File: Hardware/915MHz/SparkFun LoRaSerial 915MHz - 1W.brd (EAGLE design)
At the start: 50.8 x 27.9 mm, 75 parts, among them J1 QWIIC_RIGHT_ANGLE, J3 USB C, J4 JTAG, U2 ATSAMD21G-A, U3 AP2112K-3.3, U4 E19-915M30S, Y1 32.768kHz

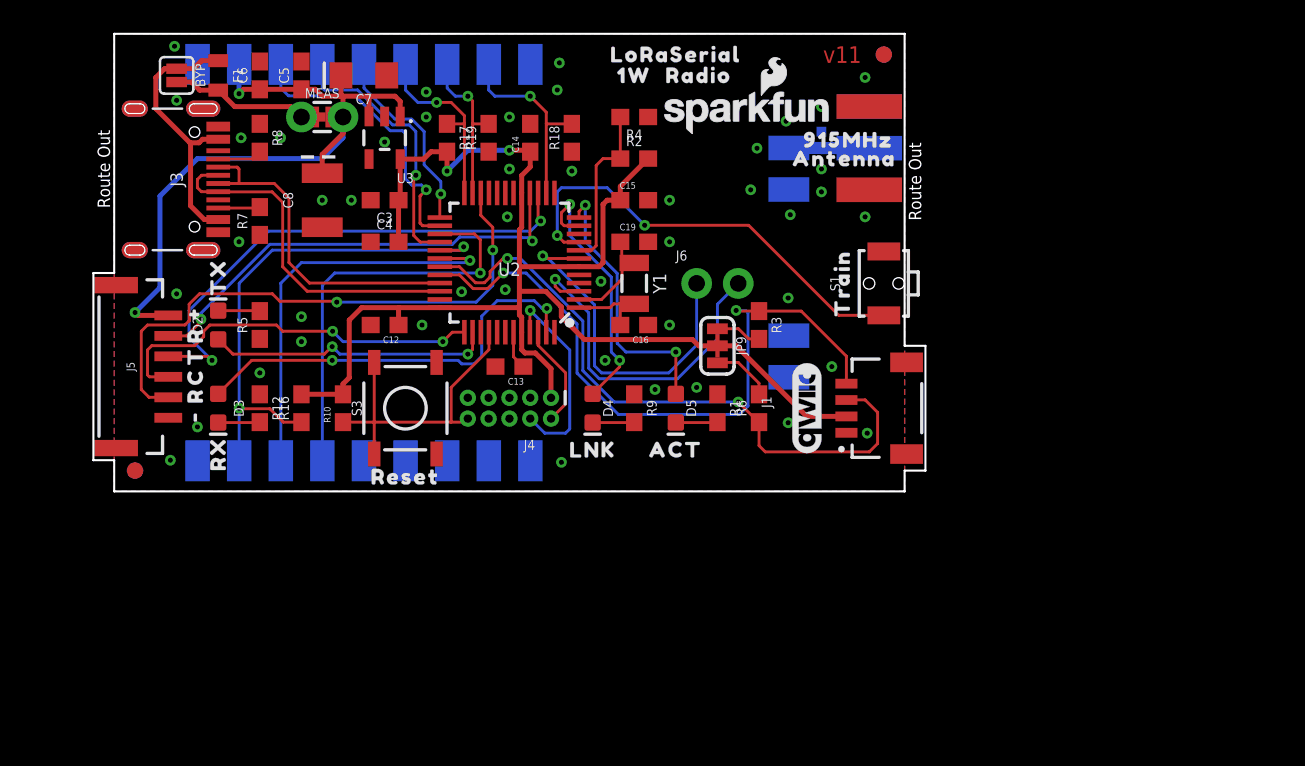
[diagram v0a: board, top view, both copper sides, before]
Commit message: Add sub folders for other frequencies
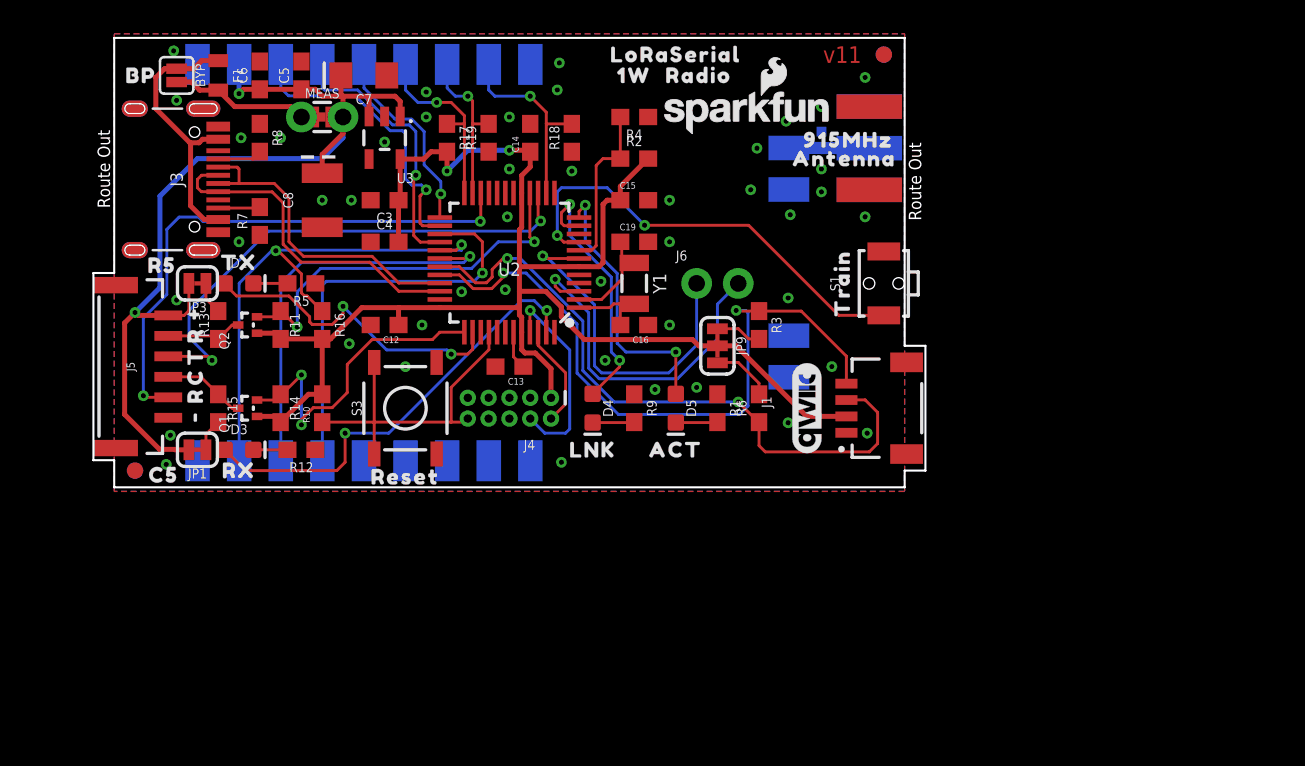
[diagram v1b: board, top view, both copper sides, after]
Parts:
- added JP1, JP3: JUMPER-SMT_2_NC_TRACE_SILK, SparkFun-Jumpers:SMT-JUMPER_2_NC_TRACE_SILK
- added Q1, Q2: 20V/0.2A/8MHz/1.2Ω/1Vth, SparkFun-DiscreteSemi:SOT-416FL
- added R11, R13, R14, R15: 2.2k, SparkFun-Resistors:0603
- added U$19: (no value), output:C50
- added U$20: (no value), output:R50
- added U$8: (no value), output:BP0
- moved R16 5.24 mm to (14.0, 10.2), turned to 270 degrees
- moved R12 3.59 mm to (12.7, 2.54), turned to 180 degrees
- moved R5 3.59 mm to (12.7, 12.7), turned to 180 degrees
- moved D3 2.84 mm to (8.89, 2.54), turned to 0 degrees
- moved D2 2.84 mm to (8.89, 12.7), turned to 0 degrees
- moved U$10 1.63 mm to (8.89, 1.27), turned to 0 degrees
- moved U$11 1.55 mm to (8.89, 14.0), turned to 0 degrees
- moved R10 1.27 mm to (14.0, 5.08)
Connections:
- removed net D30/CTS-I: J5.4, U2.37
- removed net RX-I: J5.2, U2.16
- new net CTS-I_HV: J5.4, Q1.3, R15.1
- new net D30/CTS-I_LV: Q1.2, R14.1, U2.37
- new net N$5: JP3.1, R13.2
- new net N$6: JP1.1, R15.2
- new net RX-I_HV: J5.2, Q2.3, R13.1
- new net RX-I_LV: Q2.2, R11.1, U2.16
- net 3.3V: now also Q1.1, Q2.1, R11.2, R14.2
- net 5V: now also JP1.2, JP3.2
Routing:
- net RX-I: track 28.1 -> 0.00 mm, vias 2 -> 0
- net RX-I_LV: track 0.00 -> 24.0 mm, vias 0 -> 2
- net D30/CTS-I: track 23.7 -> 0.00 mm, vias 2 -> 0
- net D30/CTS-I_LV: track 0.00 -> 19.9 mm, vias 0 -> 2
- net 5V: track 45.3 -> 59.6 mm
- net 3.3V: track 87.1 -> 94.4 mm
- net CTS-I_HV: track 0.00 -> 5.06 mm
- net RX-I_HV: track 0.00 -> 4.70 mm
- net D31/TX_LED: track 17.5 -> 19.5 mm
- net N$6: track 0.00 -> 2.00 mm
- net N$5: track 0.00 -> 2.00 mm
- net A5/RX_LED: track 25.7 -> 27.1 mm
- net D38/RTS-O: track 35.0 -> 33.6 mm
- net SAMD_!RESET!: track 19.8 -> 21.1 mm
- net D6/LORA_!RST!: track 31.3 -> 32.1 mm
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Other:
- board size 50.8 x 27.9 mm -> 50.8 x 27.4 mm

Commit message: Add RSSI LEDs
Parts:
- added D1, D7, D8: GREEN, SparkFun-LED:LED-0603
- added R20, R21, R22: 4.7k, SparkFun-Resistors:0603
- added U$21: (no value), output:RSSI0
- added U$22: (no value), output:10
- added U1: ESP32, SparkFun-RF:QFN48-0.4MM
- added U5: ESP-WROOM-3232D, SparkFun-RF:ESP-WROOM-32D
- D2: value GREEN -> BLUE
- D4: value BLUE -> GREEN
- R5: value 4.7k -> 1k
- R9: value 1k -> 4.7k
- U$6: device output:ACT3 -> output:01
- U$7: device output:LNK2 -> output:PWR0
- moved R1 21.9 mm to (17.8, 13.3), turned to 180 degrees
- moved D5 20.4 mm to (17.8, 15.0), turned to 180 degrees
- moved U$7 20.2 mm to (14.2, 14.5)
- moved U$6 12.5 mm to (39.4, 14.5)
- moved R9 3.81 mm to (33.0, 1.27), turned to 0 degrees
- moved D4 3.81 mm to (34.3, 5.08)
- moved R6 2.84 mm to (41.9, 7.62), turned to 180 degrees
- moved C4 1.40 mm to (17.8, 16.6)
- moved R3 1.27 mm to (41.9, 10.2), turned to 180 degrees
- moved LOGO3 0.76 mm to (44.3, 5.08)
- moved C3 0.63 mm to (17.8, 18.4)
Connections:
- removed net A3/TRAIN: S1.1, U2.9
- removed net A4: U2.10
- removed net D4: U2.13
- removed net D8/LINK: D4.A, U2.11
- removed net D9/ACT: D5.A, U2.12
- new net A3/RSSI1: D1.A, U2.9
- new net A4/RSSI2: D4.A, U2.10
- new net D4/TRAIN: S1.1, U2.13
- new net D8/RSSI3: D7.A, U2.11
- new net D9/RSSI4: D8.A, U2.12
- new net N$10: D7.C, R21.2
- new net N$11: D8.C, R22.2
- new net N$9: D1.C, R20.2
- net 3.3V: now also D5.A
- net GND: now also R20.1, R21.1, R22.1
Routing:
- net D4/TRAIN: track 0.00 -> 33.1 mm
- net A3/TRAIN: track 27.4 -> 0.00 mm, vias 2 -> 0
- net D8/RSSI3: track 0.00 -> 20.9 mm, vias 0 -> 2
- net D9/RSSI4: track 0.00 -> 20.8 mm, vias 0 -> 2
- net D9/ACT: track 16.5 -> 0.00 mm, vias 2 -> 0
- net D8/LINK: track 16.0 -> 0.00 mm, vias 2 -> 0
- net A4/RSSI2: track 0.00 -> 14.4 mm, vias 0 -> 2
- net A3/RSSI1: track 0.00 -> 13.3 mm, vias 0 -> 2
- net D21/SCL: track 41.3 -> 37.6 mm
- net N$9: track 0.00 -> 3.11 mm
- net N$10: track 0.00 -> 3.11 mm
- net N$11: track 0.00 -> 3.11 mm
- net D20/SDA: track 39.9 -> 37.7 mm, vias 2 -> 3
- net 3.3V: track 94.4 -> 95.9 mm
- net N$7: track 2.55 -> 1.66 mm
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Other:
- board text added: "v12"
- board text removed: "v11"

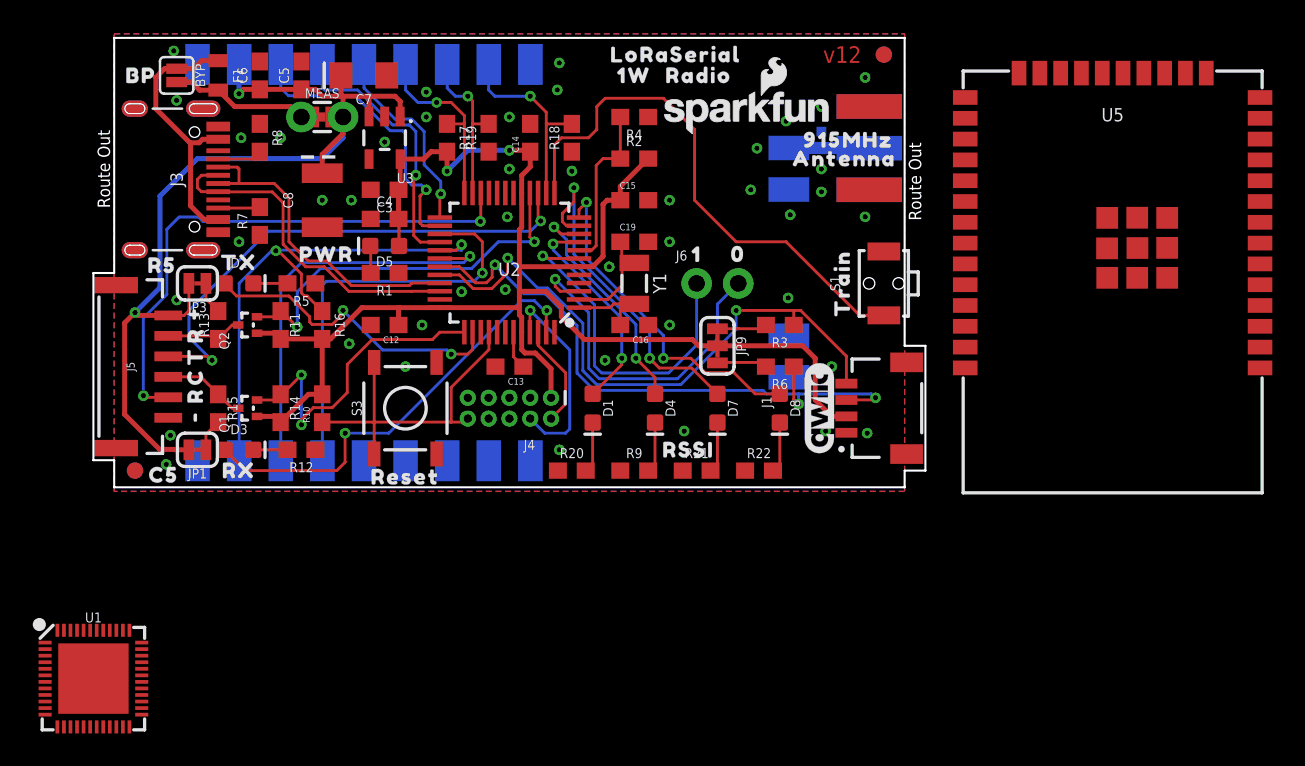
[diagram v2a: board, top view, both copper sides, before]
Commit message: Add RSSI LEDs
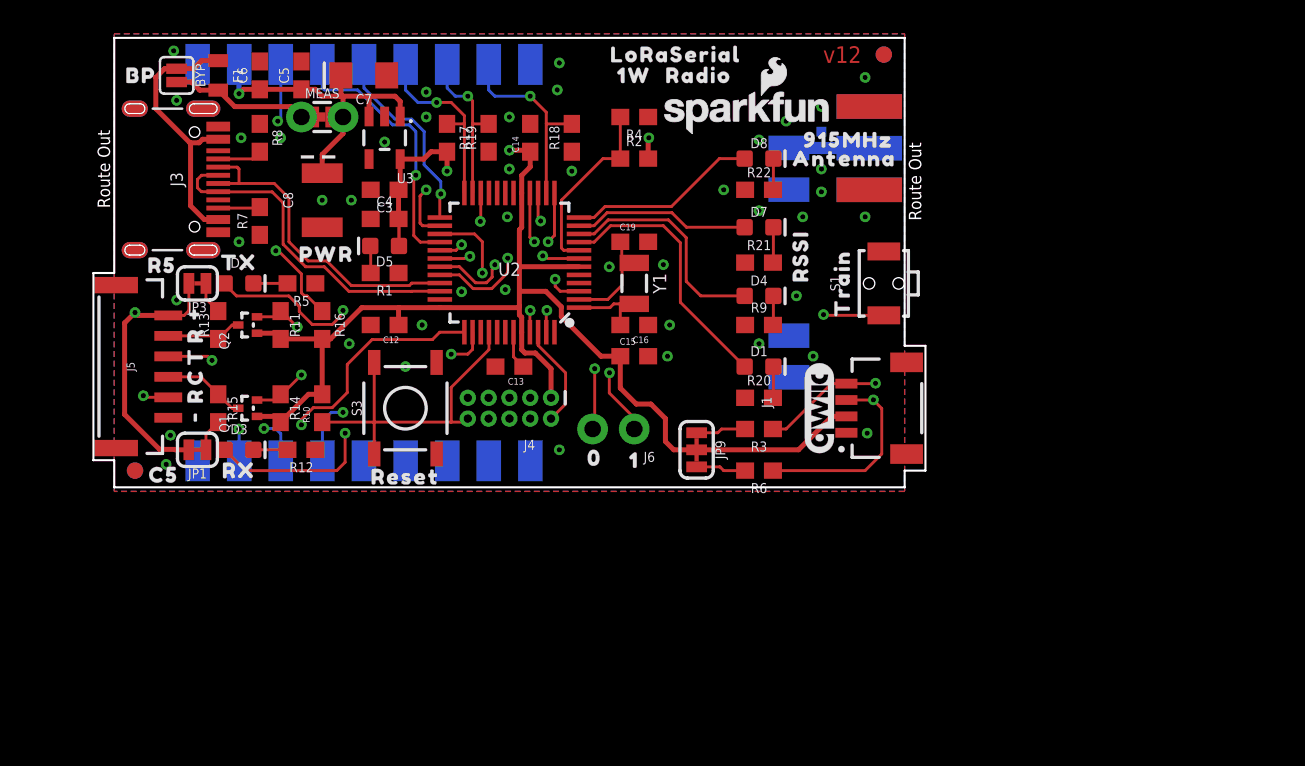
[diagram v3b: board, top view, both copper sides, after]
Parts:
- removed U1: ESP32, SparkFun-RF:QFN48-0.4MM
- removed U5: ESP-WROOM-3232D, SparkFun-RF:ESP-WROOM-32D
- moved R22 17.1 mm to (40.6, 18.4)
- moved D8 15.3 mm to (40.6, 20.3), turned to 0 degrees
- moved U$6 15.2 mm to (30.6, 2.03)
- moved U$21 13.7 mm to (43.2, 14.4), turned to 90 degrees
- moved R21 13.3 mm to (40.6, 14.0)
- moved U$22 13.1 mm to (33.0, 1.91)
- moved R20 12.3 mm to (40.6, 5.71)
- moved R9 11.7 mm to (40.6, 10.2)
- moved D7 11.3 mm to (40.6, 16.1), turned to 0 degrees
- moved D1 10.5 mm to (40.6, 7.62), turned to 0 degrees
- moved J6 9.67 mm to (33.0, 3.81), turned to 180 degrees
- moved C15 9.53 mm to (33.0, 8.26)
- moved D4 9.35 mm to (40.6, 11.9), turned to 0 degrees
- moved JP9 6.48 mm to (36.8, 2.54)
- moved R3 6.48 mm to (40.6, 3.81)
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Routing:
- net D8/RSSI3: track 20.9 -> 10.8 mm, vias 2 -> 0
- net D9/RSSI4: track 20.8 -> 11.6 mm, vias 2 -> 0
- net A0: track 21.3 -> 12.2 mm, vias 1 -> 2
- net D20/SDA: track 37.7 -> 45.8 mm, vias 3 -> 2
- net D4/TRAIN: track 33.1 -> 25.5 mm, vias 0 -> 2
- net A1: track 21.3 -> 15.3 mm, vias 1 -> 2
- net D21/SCL: track 37.6 -> 41.5 mm
- net D13/SPI_SCK: track 18.0 -> 21.3 mm, vias 1 -> 2
- net A3/RSSI1: track 13.3 -> 16.2 mm, vias 2 -> 0
- net 3.3V: track 95.9 -> 98.9 mm, vias 2 -> 3
- net N$8: track 3.11 -> 1.79 mm
- net D7/LORA_D0: track 25.0 -> 26.2 mm, vias 1 -> 2
- net N$9: track 3.11 -> 1.92 mm
- net N$11: track 3.11 -> 1.92 mm
- net A2/BOARD_ID: track 10.3 -> 11.2 mm
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- added copper zone on layer 15, net GND
- added copper zone on layer 2, net GND
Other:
- board text added: "4-Layer PCB 1.6mm Thickness 1oz Copper HASL RoHS Finish"
- board text removed: "2-Layer PCB 1.6mm Thickness 1oz Copper HASL RoHS Finish"

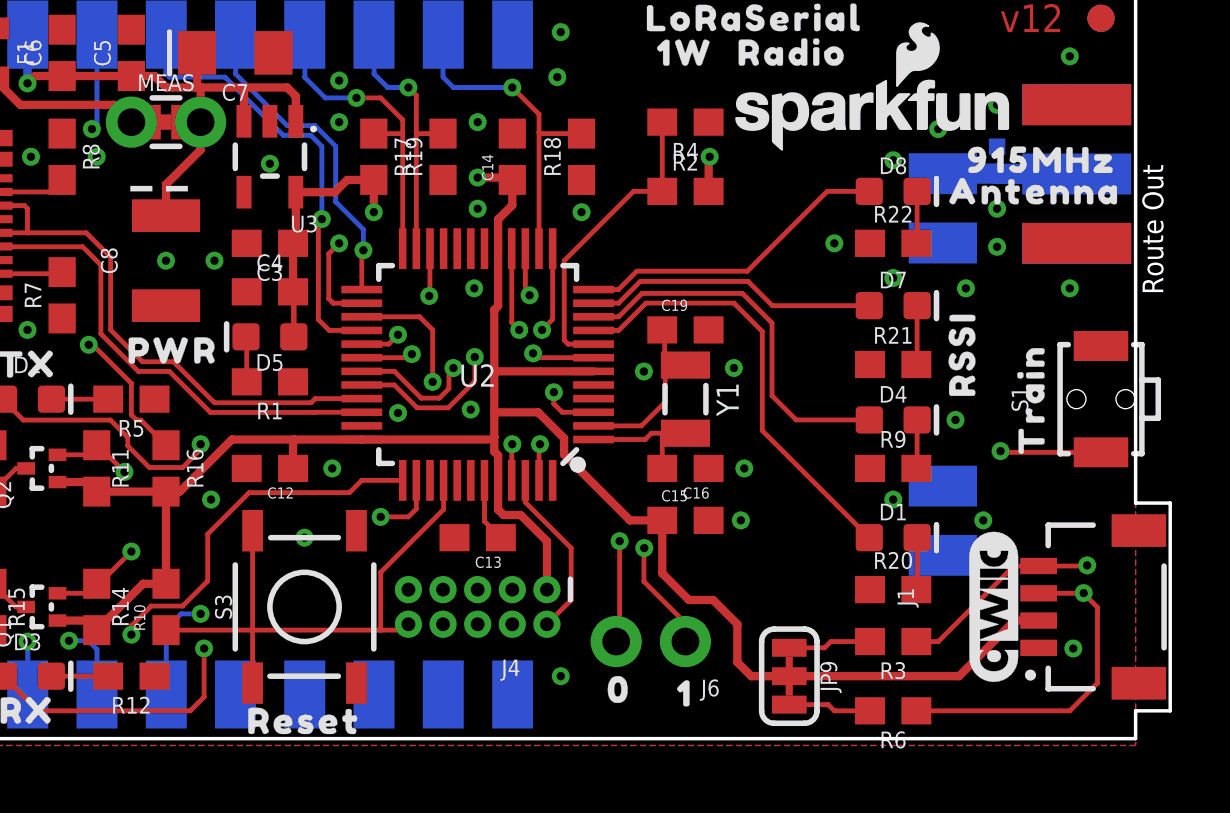
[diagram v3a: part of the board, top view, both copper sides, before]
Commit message: Adjust 50ohm microstrip for four layer
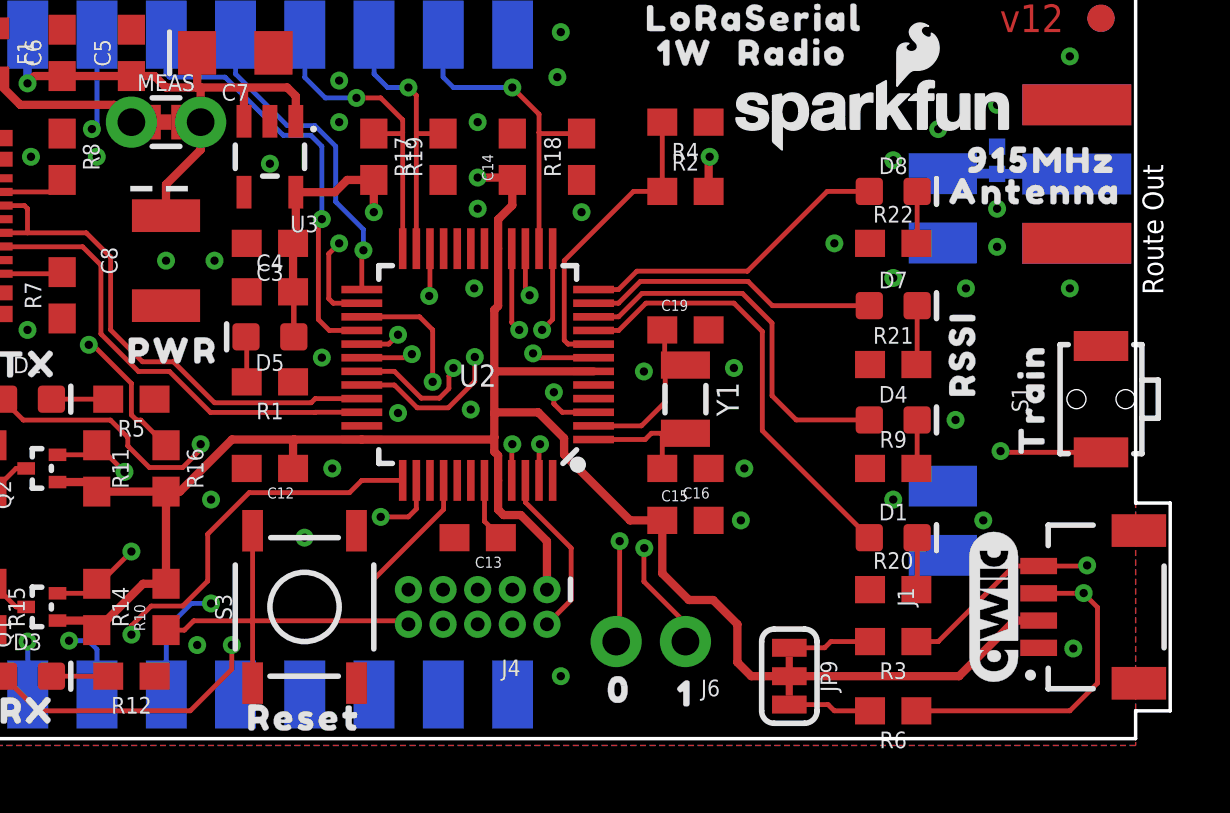
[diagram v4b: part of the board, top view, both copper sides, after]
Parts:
- moved U$2 0.13 mm to (19.1, 1.02)
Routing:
- net D10/LORA_D1: track 25.8 -> 26.6 mm
- net A5/RX_LED: track 27.1 -> 26.6 mm
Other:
- board text added: "4-Layer PCB JLC7628 Impedance Controlled 1.6mm Thickness 1oz Copper HASL RoHS Finish"
- board text removed: "4-Layer PCB 1.6mm Thickness 1oz Copper HASL RoHS Finish"
